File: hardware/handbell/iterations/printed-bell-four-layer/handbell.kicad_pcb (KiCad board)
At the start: 4 copper layers, 44.5 x 48.3 mm, 104 parts, among them IC1 RP2040_QFN56, IC4 LSM6DSOXTR, J1 504050-0291, J2 SM02B-SRSS-TB, Q1 AO3401, Q2 AO3400A, Q3 DMP2045UFY4, Q4 AO3400A, Q5 CSD83325L, U1 W25Q16JVUXIQ TR / 2MB, U2 RT9080-3.3, U3 MCP73831T-2ACI/OT, U4 MAX98357A, U5 TPS61023DRLR, U6 BQ29700DSER, X6 USB Type C, Y1 12MHz/CL10pF

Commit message: Accept paired C12 feed replacement and ground closure
Promote exact 42-open board with one ordinary power via, preserving local decoupling copper and private returns. Review local antipad and bounded refill differences; release only a bounded ordinary C24 ground connection next.

Co-authored-by: Copilot <223556219+Copilot@users.noreply.github.com>
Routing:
- net +3V3: track 178.3 -> 173.2 mm, vias 14 -> 15
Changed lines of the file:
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@@
 (segment (start 90.955400 94.507700) (end 92.004100 94.507700) (width 0.1778) (layer "F.Cu") (net "+3V3"))
 (segment (start 90.940400 94.492700) (end 90.955400 94.507700) (width 0.1778) (layer "F.Cu") (net "+3V3"))
-(segment (start 97.876500 94.507700) (end 92.004100 94.507700) (width 0.1778) (layer "F.Cu") (net "+3V3"))
 (segment (start 99.000000 95.631200) (end 97.876500 94.507700) (width 0.1778) (layer "F.Cu") (net "+3V3"))
 (segment (start 90.412300 94.492700) (end 90.940400 94.492700) (width 0.1778) (layer "F.Cu") (net "+3V3"))
@@
 (segment (start 87.700000 88.950000) (end 89.700000 88.950000) (width 0.200000) (layer "In2.Cu") (net "USBBOOT"))
 (segment (start 89.700000 88.950000) (end 92.850000 92.100000) (width 0.200000) (layer "In2.Cu") (net "USBBOOT"))
+(segment (start 97.876500 94.507700) (end 97.876500 94.757700) (width 0.200000) (layer "F.Cu") (net "+3V3"))
+(via (at 97.876500 94.757700) (size 0.604000) (drill 0.350000) (layers "F.Cu" "B.Cu") (net "+3V3"))
+(segment (start 97.876500 94.757700) (end 97.876500 94.250000) (width 0.400000) (layer "In2.Cu") (net "+3V3"))
 )

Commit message: Accept C24 ground via with explicit filled and capped process
Promote exact 41-open board, retaining land/mask/paste and plane geometry. Bind C24 via treatment alongside U4 requirements; supplier, stencil, yield and cost remain unqualified. Refresh remaining-routing handoff.

Co-authored-by: Copilot <223556219+Copilot@users.noreply.github.com>
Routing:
- net GND: vias 23 -> 24
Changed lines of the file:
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@@
 (via (at 97.876500 94.757700) (size 0.604000) (drill 0.350000) (layers "F.Cu" "B.Cu") (net "+3V3"))
 (segment (start 97.876500 94.757700) (end 97.876500 94.250000) (width 0.400000) (layer "In2.Cu") (net "+3V3"))
+(via (at 92.004083 93.491669) (size 0.600000) (drill 0.300000) (layers "F.Cu" "B.Cu") (net "GND"))
 )

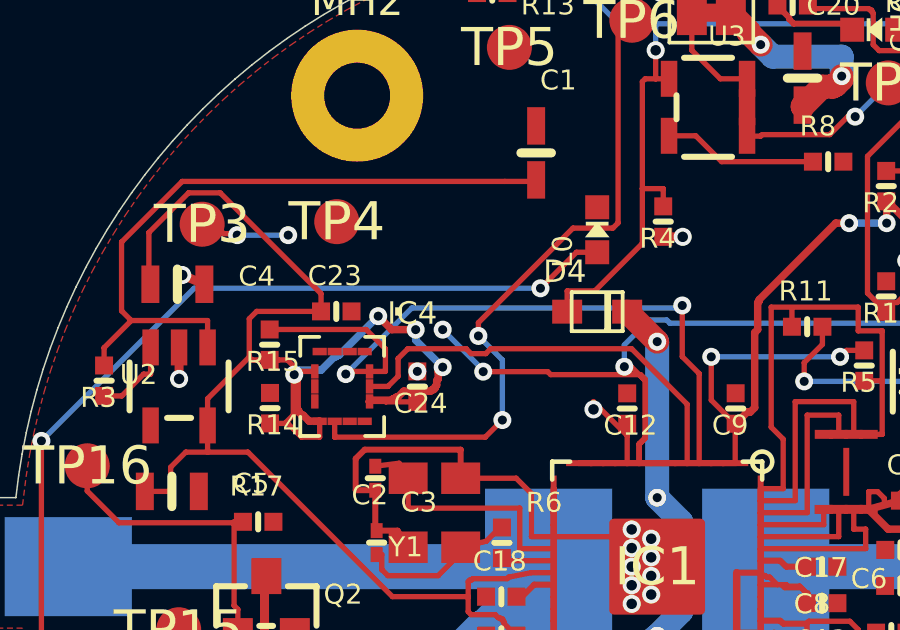
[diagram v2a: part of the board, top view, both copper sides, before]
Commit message: Accept integrated IMU routing and its exact CAD manifest bridge
Co-authored-by: Copilot <223556219+Copilot@users.noreply.github.com>
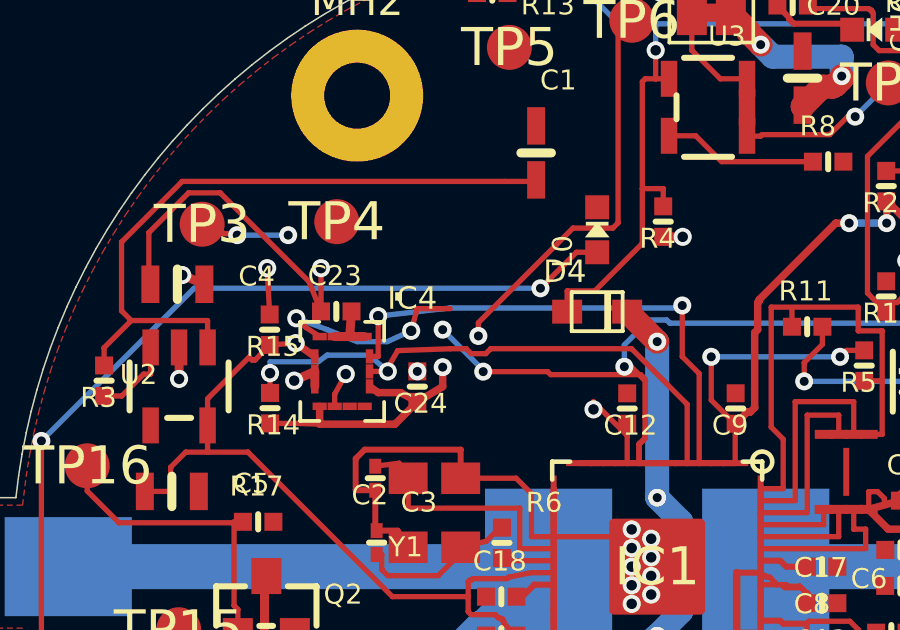
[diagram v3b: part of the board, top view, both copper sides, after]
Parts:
- moved IC4 0.50 mm to (89.5, 93.5)
- moved R15 0.50 mm to (87.1, 92.1)
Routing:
- net INT: track 0.00 -> 6.91 mm, vias 0 -> 2
- net SCL: track 14.3 -> 19.1 mm, vias 0 -> 2
- net /IMU_INT2: track 22.9 -> 19.4 mm
- net GND: track 117.4 -> 120.5 mm, vias 24 -> 25
- net SDA: track 23.9 -> 25.3 mm, vias 2 -> 3
- net +3V3: track 173.2 -> 171.9 mm, vias 15 -> 14
